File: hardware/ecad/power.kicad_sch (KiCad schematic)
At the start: 22 parts, among them J1 USB_C_Receptacle, J2 Conn_01x02, U1 BQ24079RGTT, U2 TPS62162DSG, U3 TLV61047DDC

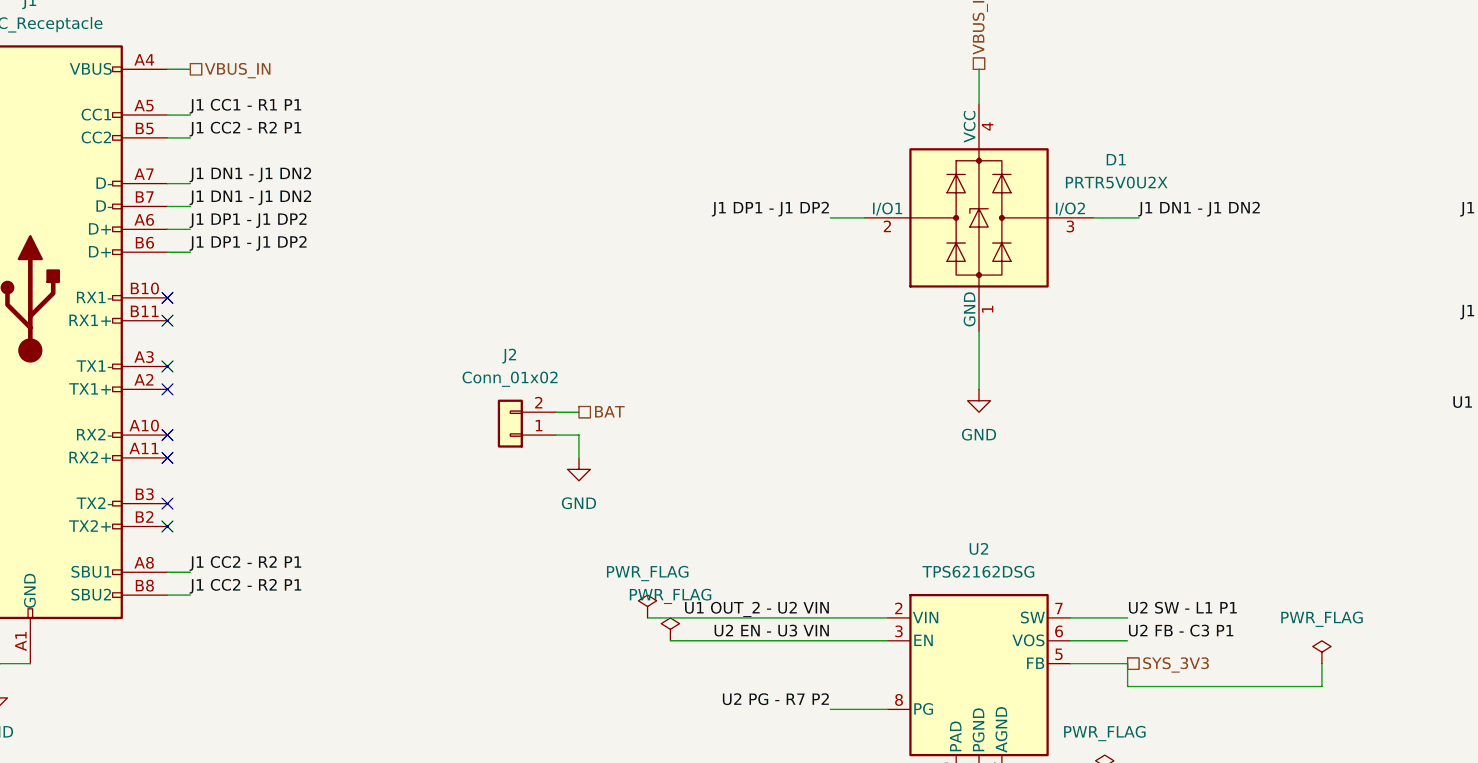
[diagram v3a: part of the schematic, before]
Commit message: feat: complete schematic design for midi2BLE v1
- Add 7-sheet hierarchical schematic covering full system architecture
- Power sheet: BQ24079RGTT charger, TPS62162DSG 3.3V buck, TLV61047DDC
  5V boost, PRTR5V0U2X ESD protection, USB-C receptacle with CC resistors
- ESP32-S3 sheet: WROOM-1-N8R2 module, UART header, boot/reset buttons,
  MODE_SEL debounce circuit, BAT_SENSE ADC input
- OLED UI sheet: SPI SSD1306 connector (GPIO35/36/10/9/8)
- Battery sense sheet: resistor divider for ADC1 battery voltage monitoring
- VBUS switching sheet: TPS2116DRL power mux for BOOST_5V/VBUS_IN selection
- USB data sheet: TS3USB30EDGSR USB 2.0 mux, keyboard USB-B connector,
  PRTR5V0U2X ESD protection on keyboard data lines
- Fix OLED from I2C to SPI, reassign GPIO11/12 away from octal flash
- Fix BQ24079 TS pin from VBUS_IN to 10k resistor to GND
- Set ISET=590R (1.5A charge), ILIM=1k (1.55A input limit) for 2500-3000mAh LiPo
- Pass ERC with 0 errors, 0 warnings (6 ignored: BQ24079 symbol quirks)
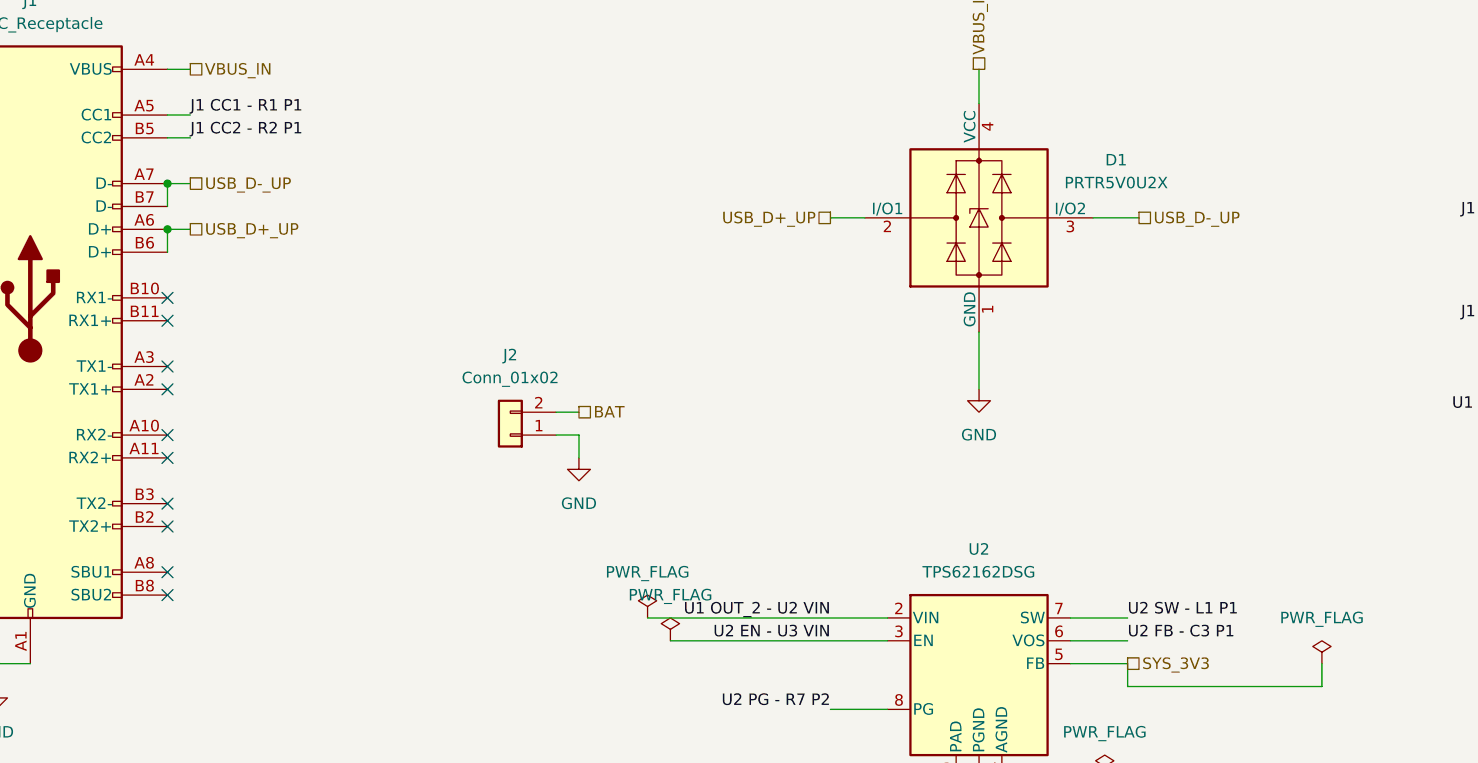
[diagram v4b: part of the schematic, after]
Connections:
- net J1 CC2 - R2 P1: no longer J1.A8 (SBU1), J1.B8 (SBU2)
- net J1 DN1 - J1 DN2 renamed USB_D-_UP
- net J1 DP1 - J1 DP2 renamed USB_D+_UP
- no-connect marks 9 -> 11
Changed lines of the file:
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@@
+	)
+	(junction
+		(at 52.07 43.18)
+		(diameter 0)
+		(color 0 0 0 0)
 	)
 	(junction
@@
 		(color 0 0 0 0)
 	)
+	(junction
+		(at 52.07 38.1)
+		(diameter 0)
+		(color 0 0 0 0)
+	)
+	(no_connect
+		(at 52.07 81.28)
+	)
 	(no_connect
 		(at 52.07 68.58)
@@
 	)
 	(no_connect
+		(at 52.07 83.82)
+	)
+	(no_connect
 		(at 52.07 50.8)
 	)
@@
 	(wire
 		(pts
-			(xy 54.61 45.72) (xy 52.07 45.72)
-		)
-		(stroke
-			(width 0)
-			(type default)
-		)
-	)
-	(wire
-		(pts
 			(xy 156.21 105.41) (xy 142.24 105.41)
 		)
@@
 	(wire
 		(pts
+			(xy 52.07 38.1) (xy 52.07 40.64)
+		)
+		(stroke
+			(width 0)
+			(type default)
+		)
+	)
+	(wire
+		(pts
 			(xy 271.78 41.91) (xy 280.67 41.91)
 		)
@@
 	(wire
 		(pts
-			(xy 54.61 81.28) (xy 52.07 81.28)
-		)
-		(stroke
-			(width 0)
-			(type default)
-		)
-	)
-	(wire
-		(pts
 			(xy 226.06 41.91) (xy 234.95 41.91)
 		)
@@
 	(wire
 		(pts
-			(xy 54.61 83.82) (xy 52.07 83.82)
-		)
-		(stroke
-			(width 0)
-			(type default)
-		)
-	)
-	(wire
-		(pts
 			(xy 60.96 157.48) (xy 62.23 157.48)
 		)
@@
 	(wire
 		(pts
-			(xy 54.61 40.64) (xy 52.07 40.64)
-		)
-		(stroke
-			(width 0)
-			(type default)
-		)
-	)
-	(wire
-		(pts
 			(xy 273.05 124.46) (xy 281.94 124.46)
 		)
@@
 		(pts
 			(xy 271.78 53.34) (xy 280.67 53.34)
+		)
+		(stroke
+			(width 0)
+			(type default)
+		)
+	)
+	(wire
+		(pts
+			(xy 52.07 43.18) (xy 52.07 45.72)
 		)
 		(stroke
@@
 		)
 	)
-	(label "J1 DP1 - J1 DP2"
-		(at 125.73 41.91 180)
-		(effects
-			(font
-				(size 1.27 1.27)
-			)
-			(justify right bottom)
-		)
-	)
 	(label "L2 P2 - C4 P1"
 		(at 254 30.48 180)
@@
 		)
 	)
-	(label "J1 DP1 - J1 DP2"
-		(at 54.61 43.18 0)
-		(effects
-			(font
-				(size 1.27 1.27)
-			)
-			(justify left bottom)
-		)
-	)
 	(label "U1 OUT_2 - U2 VIN"
 		(at 81.28 133.35 0)
@@
 		)
 	)
-	(label "J1 DN1 - J1 DN2"
-		(at 160.02 41.91 0)
-		(effects
-			(font
-				(size 1.27 1.27)
-			)
-			(justify left bottom)
-		)
-	)
 	(label "J1 CC2 - R2 P1"
 		(at 54.61 33.02 0)
@@
 		)
 	)
-	(label "J1 DN1 - J1 DN2"
-		(at 54.61 38.1 0)
-		(effects
-			(font
-				(size 1.27 1.27)
-			)
-			(justify left bottom)
-		)
-	)
 	(label "U1 ILIM - R4 P1"
 		(at 38.1 134.62 180)
@@
 		)
 	)
-	(label "J1 CC2 - R2 P1"
-		(at 54.61 81.28 0)
-		(effects
-			(font
-				(size 1.27 1.27)
-			)
-			(justify left bottom)
-		)
-	)
 	(label "U1 OUT_2 - U2 VIN"
 		(at 125.73 86.36 180)
@@
 		)
 	)
-	(label "J1 DN1 - J1 DN2"
-		(at 54.61 40.64 0)
-		(effects
-			(font
-				(size 1.27 1.27)
-			)
-			(justify left bottom)
-		)
-	)
 	(label "U1 ILIM - R4 P1"
 		(at 254 41.91 180)
@@
 		)
 	)
-	(label "J1 CC2 - R2 P1"
-		(at 54.61 83.82 0)
-		(effects
-			(font
-				(size 1.27 1.27)
-			)
-			(justify left bottom)
-		)
-	)
-	(label "J1 DP1 - J1 DP2"
-		(at 54.61 45.72 0)
-		(effects
-			(font
-				(size 1.27 1.27)
-			)
-			(justify left bottom)
-		)
-	)
 	(label "U2 SW - L1 P1"
 		(at 158.75 86.36 0)
@@
 		)
 	)
+	(hierarchical_label "USB_D+_UP"
+		(shape passive)
+		(at 54.61 43.18 0)
+		(effects
+			(font
+				(size 1.27 1.27)
+			)
+			(justify left)
+		)
+	)
 	(hierarchical_label "VBUS_IN"
 		(shape passive)
@@
 		)
 	)
+	(hierarchical_label "USB_D+_UP"
+		(shape passive)
+		(at 125.73 41.91 180)
+		(effects
+			(font
+				(size 1.27 1.27)
+			)
+			(justify right)
+		)
+	)
 	(hierarchical_label "VBUS_IN"
 		(shape passive)
@@
 		)
 	)
+	(hierarchical_label "USB_D-_UP"
+		(shape passive)
+		(at 160.02 41.91 0)
+		(effects
+			(font
+				(size 1.27 1.27)
+			)
+			(justify left)
+		)
+	)
 	(hierarchical_label "BAT"
 		(shape passive)
@@
 		(effects
 			(font
+				(size 1.27 1.27)
+			)
+			(justify left)
+		)
+	)
+	(hierarchical_label "USB_D-_UP"
+		(shape passive)
+		(at 54.61 38.1 0)
+		(effects
+			(font

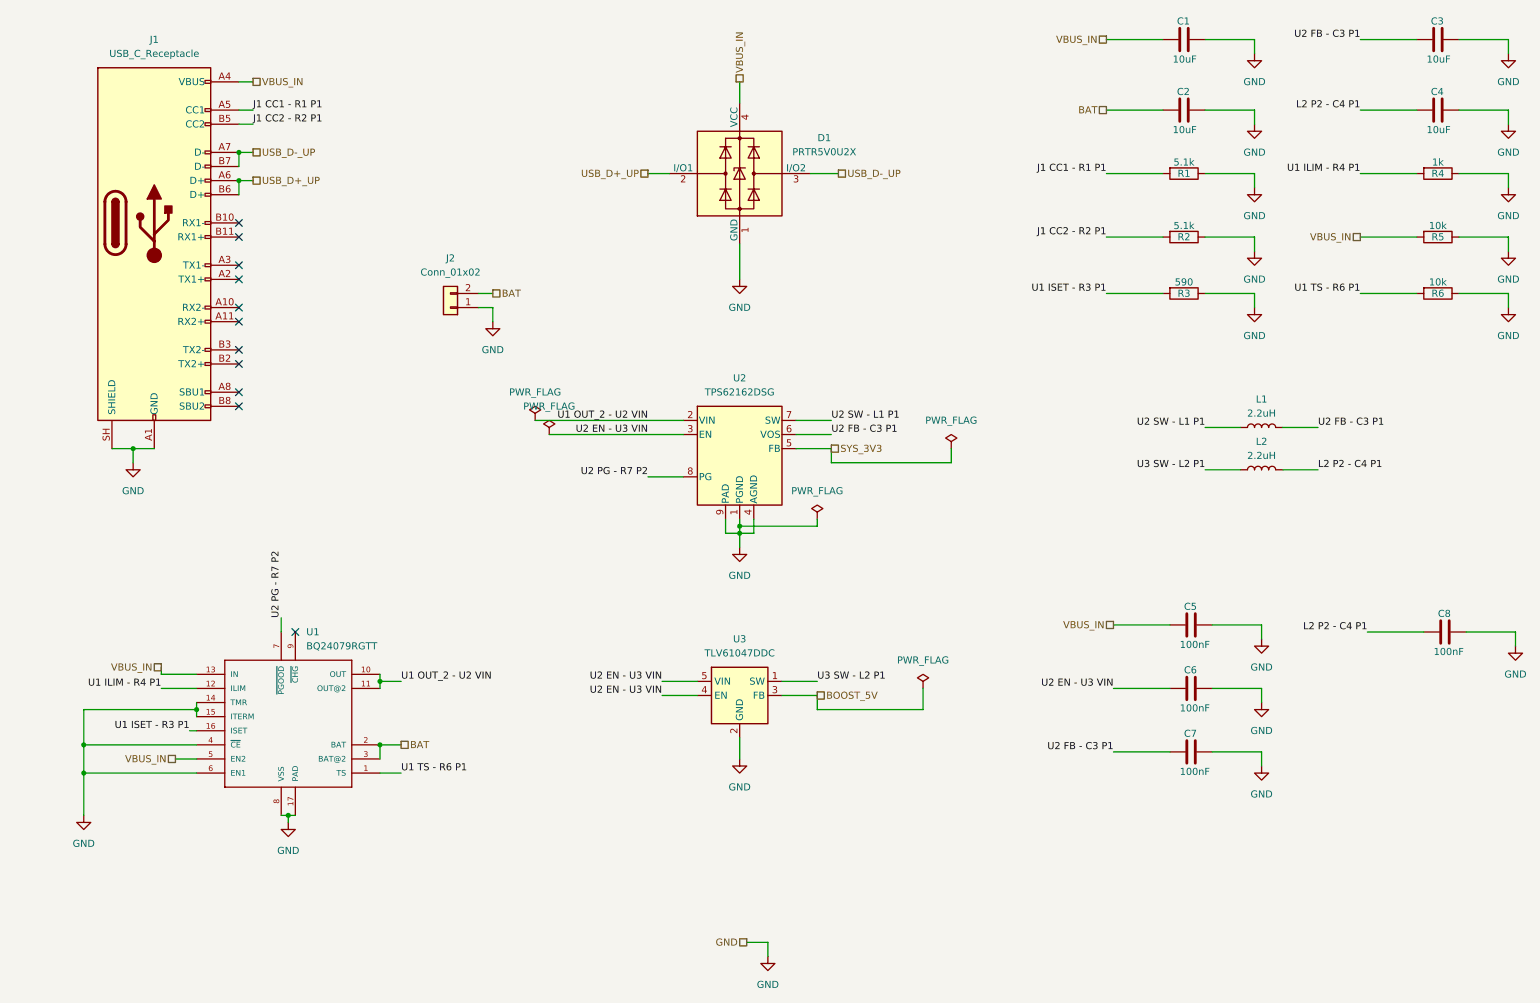
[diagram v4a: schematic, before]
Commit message: Updated schematics and added printed pdf
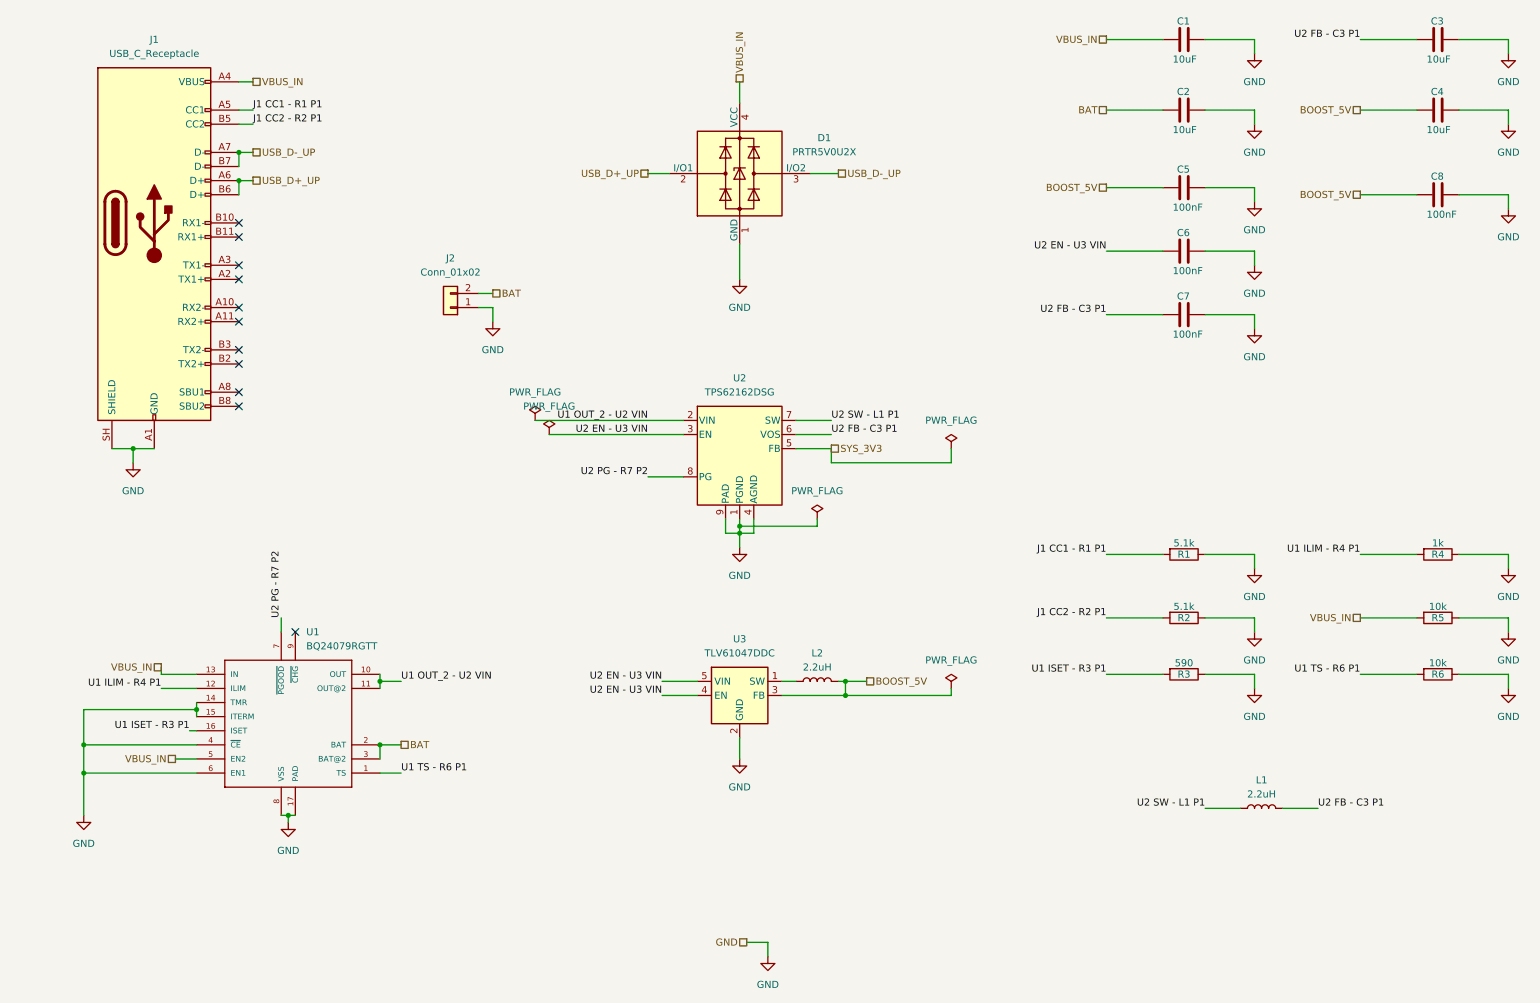
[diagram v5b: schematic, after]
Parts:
- C5, C6, C7, C8: footprint Capacitor_SMD:C_0603_1608Metric -> Capacitor_SMD:C_0402_1005Metric
- L1, L2: footprint Inductor_SMD:L_0603_1608Metric -> Inductor_SMD:L_1008_2520Metric
- R1, R2, R3, R4, R5, R6: footprint Resistor_SMD:R_0201_0603Metric -> Capacitor_SMD:C_0402_1005Metric
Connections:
- net L2 P2 - C4 P1 is gone; now on net BOOST_5V: C4.2, C8.2, L2.2
- net BOOST_5V: now also C5.2
- net VBUS_IN: no longer C5.2
- net U3 SW - L2 P1: no longer names the net of L2.1, U3.1 (SW)
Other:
- moved on the sheet: L1, L2, R1, R2, R3, R4, R5, R6

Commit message: docs(hardware): update ecad README to reflect completed schematic and PCB — PCB IS DONE!!!
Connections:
- net USB_D+_UP renamed USB_UP+
- net USB_D-_UP renamed USB_UP-
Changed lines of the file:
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@@
 		)
 	)
-	(hierarchical_label "USB_D+_UP"
+	(hierarchical_label "USB_UP+"
 		(shape passive)
 		(at 54.61 43.18 0)
@@
 		)
 	)
-	(hierarchical_label "USB_D+_UP"
+	(hierarchical_label "USB_UP+"
 		(shape passive)
 		(at 125.73 41.91 180)
@@
 		)
 	)
-	(hierarchical_label "USB_D-_UP"
+	(hierarchical_label "USB_UP-"
 		(shape passive)
 		(at 160.02 41.91 0)
@@
 		)
 	)
-	(hierarchical_label "USB_D-_UP"
+	(hierarchical_label "USB_UP-"
 		(shape passive)
 		(at 54.61 38.1 0)
